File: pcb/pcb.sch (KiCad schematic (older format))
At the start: 81 parts, among them J1 USB_mini_B, K1 7, K10 6, K11 3, K12 EQUAL, K13 DEVIDE, K14 *, K15 -, K16 +, K2 4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

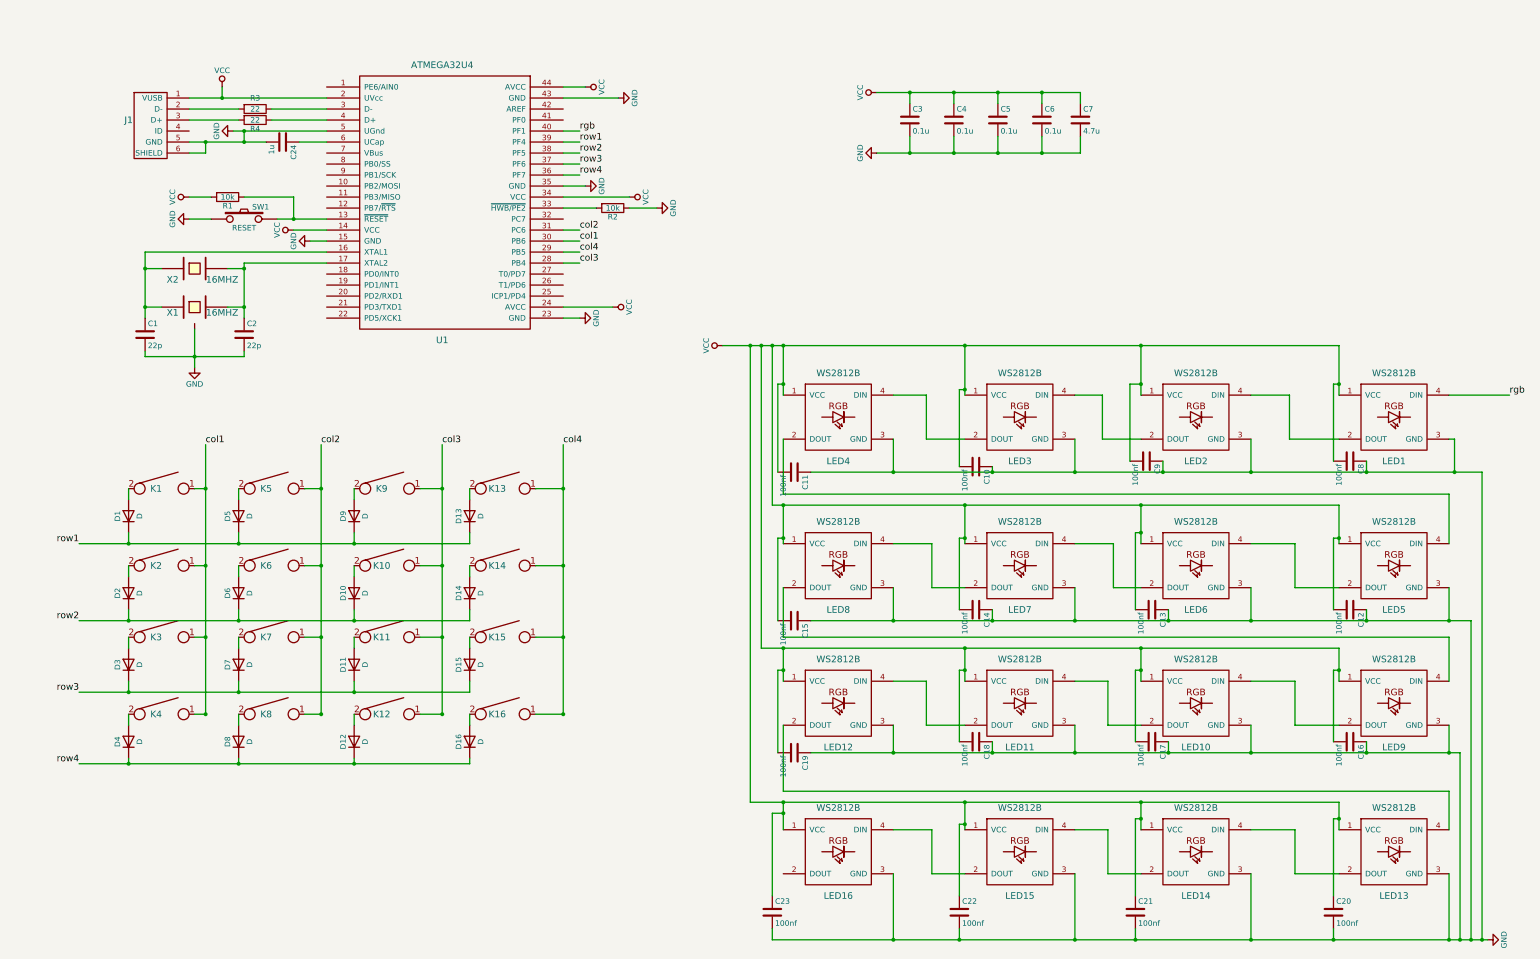
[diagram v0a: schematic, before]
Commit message: change to atmega32u2
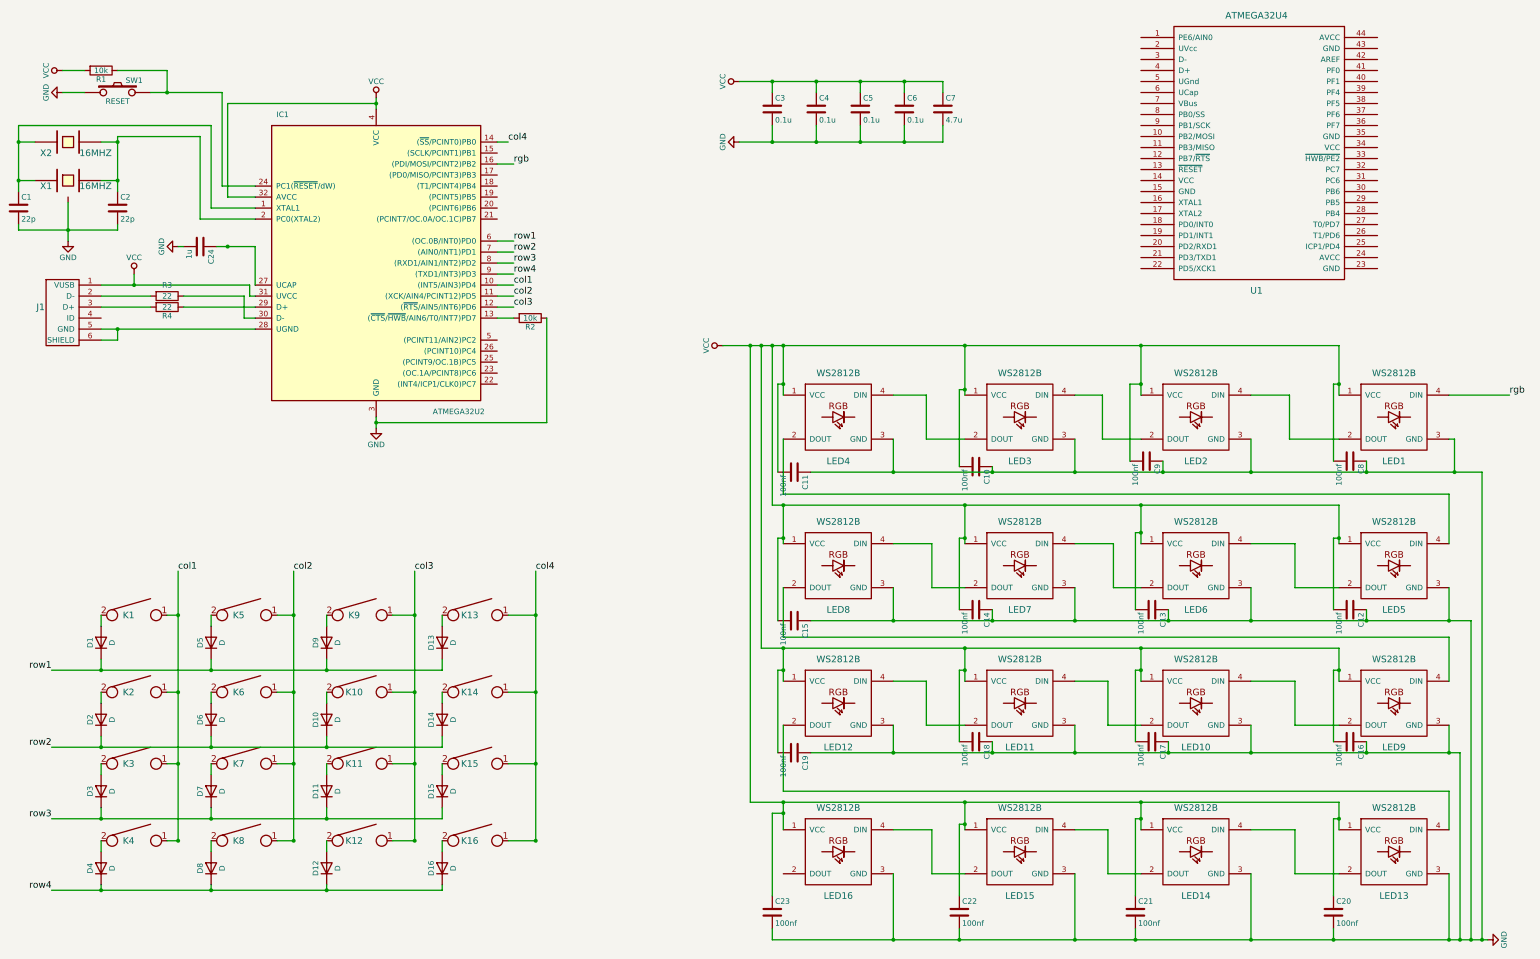
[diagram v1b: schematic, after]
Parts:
- added IC1: ATMEGA32U2, symbol ATMEGA32U2
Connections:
- net GND: now also IC1.3 (GND); no longer J1.5 (GND), J1.6 (SHIELD), U1.15 (GND), U1.23 (GND), U1.35 (GND), U1.43 (GND), U1.5 (UGnd)
- net VCC: now also IC1.31 (UVCC), IC1.32 (AVCC), IC1.4 (VCC); no longer U1.14 (VCC), U1.2 (UVcc), U1.24 (AVCC), U1.34 (VCC), U1.44 (AVCC)
- net col1: now also IC1.10 ((INT5/AIN3)PD4); no longer U1.30 (PB6)
- net col2: now also IC1.11 ((XCK/AIN4/PCINT12)PD5); no longer U1.31 (PC6)
- net col3: now also IC1.12 ((~RTS~/AIN5/INT6)PD6); no longer U1.28 (PB4)
- net col4: now also IC1.14 ((~SS~/PCINT0)PB0); no longer U1.29 (PB5)
- net rgb: now also IC1.16 ((PDI/MOSI/PCINT2)PB2); no longer U1.40 (PF1)
- net row1: now also IC1.6 ((OC.0B/INT0)PD0); no longer U1.39 (PF4)
- net row2: now also IC1.7 ((AIN0/INT1)PD1); no longer U1.38 (PF5)
- net row3: now also IC1.8 ((RXD1/AIN1/INT2)PD2); no longer U1.37 (PF6)
- net row4: now also IC1.9 ((TXD1/INT3)PD3); no longer U1.36 (PF7)
- net at R1.1, SW1.2: now also IC1.24 (PC1(~RESET~/dW)); no longer U1.13 (~RESET)
- net at C1.1, X1.1, X2.1: now also IC1.1 (XTAL1); no longer U1.16 (XTAL1)
- net at C2.1, X1.2, X2.2: now also IC1.2 (PC0(XTAL2)); no longer U1.17 (XTAL2)
- net at U1.3 (D-): no longer R3.1
- net at U1.33 (~HWB/PE2): no longer R2.2
- net at U1.4 (D+): no longer R4.1
- net at U1.6 (UCap): no longer C24.1
- new net: IC1.13 ((~CTS~/~HWB~/AIN6/T0/INT7)PD7), R2.2
- new net: IC1.28 (UGND), J1.5 (GND), J1.6 (SHIELD)
- new net: IC1.30 (D-), R3.1
- new net: IC1.29 (D+), R4.1
- new net: C24.1, IC1.27 (UCAP)
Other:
- moved on the sheet: C1, C2, C24, C3, C4, C5, C6, C7, D1, D10, D11, D12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

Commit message: rewiring
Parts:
- removed U1: ATMEGA32U4, keyboard_parts:QFP44_reflow, symbol ATMEGA32U4
- IC1: footprint (none) -> keyboard_parts:QFP32
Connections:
- net col1: now also IC1.14 ((~SS~/PCINT0)PB0); no longer IC1.10 ((INT5/AIN3)PD4)
- net col2: now also IC1.12 ((~RTS~/AIN5/INT6)PD6); no longer IC1.11 ((XCK/AIN4/PCINT12)PD5)
- net col3: now also IC1.11 ((XCK/AIN4/PCINT12)PD5); no longer IC1.12 ((~RTS~/AIN5/INT6)PD6)
- net col4: now also IC1.10 ((INT5/AIN3)PD4); no longer IC1.14 ((~SS~/PCINT0)PB0)
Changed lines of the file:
@@
 $EndDescr
-$Comp
-L ATMEGA32U4 U1
-U 1 1 58B11B4F
-P 12100 1500
-F 0 "U1" H 12100 250 60  0000 C CNN
-F 1 "ATMEGA32U4" H 12100 2750 60  0000 C CNN
-F 2 "keyboard_parts:QFP44_reflow" H 12100 1500 60  0001 C CNN
-F 3 "" H 12100 1500 60  0000 C CNN
-	1    12100 1500
-	1    0    0    -1
-$EndComp
 $Comp
 L XTAL_GND X1
@@
 Text Label 5350 2500 0    60   ~ 0
 row3
-Text Label 5350 2700 0    60   ~ 0
+Text Label 5350 1400 0    60   ~ 0
 col1
+Text Label 5350 2900 0    60   ~ 0
+col2
 Text Label 5350 2800 0    60   ~ 0
-col2
-Text Label 5350 2900 0    60   ~ 0
 col3
 $Comp
@@
 	0    -1   -1   0
 $EndComp
-Text Label 5300 1400 0    60   ~ 0
+Text Label 5350 2700 0    60   ~ 0
 col4
 Text Label 5350 2600 0    60   ~ 0
@@
 F 0 "IC1" H 3250 3850 50  0000 C CNN
 F 1 "ATMEGA32U2" H 4850 1150 50  0000 C CNN
-F 2 "" H 3950 2550 50  0000 C CNN
+F 2 "keyboard_parts:QFP32" H 3950 2550 50  0000 C CNN
 F 3 "http://www.atmel.com/Images/doc7799.pdf" H 4200 1050 50  0001 C CNN
 	1    4100 2500
@@
 Connection ~ 4100 1050
 Wire Wire Line
-	5200 2900 5350 2900
-Wire Wire Line
-	5200 2800 5350 2800
-Wire Wire Line
-	5200 2700 5350 2700
-Wire Wire Line
 	5200 2600 5350 2600
 Wire Wire Line
@@
 Wire Wire Line
 	5200 3000 5350 3000
-Wire Wire Line
-	5300 1400 5200 1400
 Wire Wire Line
 	4100 3950 5650 3950
@@
 	5650 3950 5650 3000
 Connection ~ 4100 3950
+Wire Wire Line
+	5200 2900 5350 2900
+Wire Wire Line
+	5200 2800 5350 2800
+Wire Wire Line
+	5200 2700 5350 2700
+Wire Wire Line
+	5200 1400 5350 1400
 $EndSCHEMATC
